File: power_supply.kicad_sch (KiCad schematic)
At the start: 4 parts

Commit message: All component except led matrix
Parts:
- gave numbers to parts that had none: 4
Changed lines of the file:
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@@
   (junction (at 31.75 41.275) (diameter 0) (color 0 0 0 0)
-  )
-  (junction (at 27.94 41.275) (diameter 0) (color 0 0 0 0)
   )
   (junction (at 71.12 41.275) (diameter 0) (color 0 0 0 0)
@@
   )
   (wire (pts (xy 71.12 41.275) (xy 76.2 41.275))
-    (stroke (width 0) (type default) (color 0 0 0 0))
-  )
-  (wire (pts (xy 26.67 41.275) (xy 27.94 41.275))
     (stroke (width 0) (type default) (color 0 0 0 0))
   )
@@
   (symbol (lib_id "Device:C") (at 31.75 46.355 0) (unit 1)
     (in_bom yes) (on_board yes) (fields_autoplaced)
-    (property "Reference" "C?" (id 0) (at 35.56 45.0849 0)
+    (property "Reference" "C1" (id 0) (at 35.56 45.0849 0)
       (effects (font (size 1.27 1.27)) (justify left))
     )
@@
   (symbol (lib_id "Device:R") (at 45.72 43.815 90) (unit 1)
     (in_bom yes) (on_board yes) (fields_autoplaced)
-    (property "Reference" "R?" (id 0) (at 45.72 37.465 90))
+    (property "Reference" "R1" (id 0) (at 45.72 37.465 90))
     (property "Value" "10k" (id 1) (at 45.72 40.005 90))
     (property "Footprint" "" (id 2) (at 45.72 45.593 90)
@@
   (symbol (lib_id "Device:C") (at 71.12 46.355 0) (unit 1)
     (in_bom yes) (on_board yes) (fields_autoplaced)
-    (property "Reference" "C?" (id 0) (at 74.93 45.0849 0)
+    (property "Reference" "C2" (id 0) (at 74.93 45.0849 0)
       (effects (font (size 1.27 1.27)) (justify left))
     )
@@
   (symbol (lib_id "Regulator_Linear:AP2112K-3.3") (at 58.42 43.815 0) (unit 1)
     (in_bom yes) (on_board yes) (fields_autoplaced)
-    (property "Reference" "U?" (id 0) (at 58.42 33.655 0))
+    (property "Reference" "U1" (id 0) (at 58.42 33.655 0))
     (property "Value" "AP2112K-3.3" (id 1) (at 58.42 36.195 0))
     (property "Footprint" "Package_TO_SOT_SMD:SOT-23-5" (id 2) (at 58.42 35.56 0)

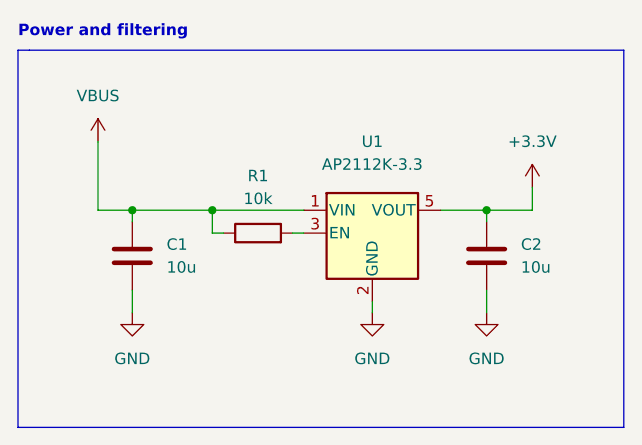
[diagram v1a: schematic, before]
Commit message: finish schematic, prep pcb
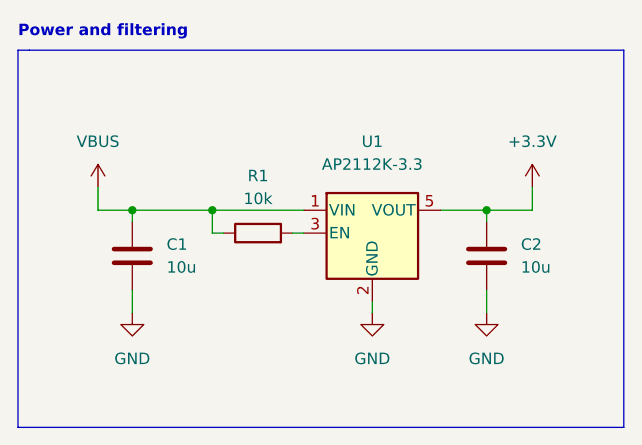
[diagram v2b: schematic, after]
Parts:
- C1, C2: footprint (none) -> Capacitor_SMD:C_0603_1608Metric
- R1: footprint (none) -> Resistor_SMD:R_0402_1005Metric
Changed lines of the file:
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@@
     (stroke (width 0) (type default) (color 0 0 0 0))
   )
-  (wire (pts (xy 27.94 33.655) (xy 27.94 41.275))
+  (wire (pts (xy 27.94 38.735) (xy 27.94 41.275))
     (stroke (width 0) (type default) (color 0 0 0 0))
   )
@@
       (effects (font (size 1.27 1.27)) (justify left))
     )
-    (property "Footprint" "" (id 2) (at 32.7152 50.165 0)
+    (property "Footprint" "Capacitor_SMD:C_0603_1608Metric" (id 2) (at 32.7152 50.165 0)
       (effects (font (size 1.27 1.27)) hide)
     )
@@
     (property "Reference" "R1" (id 0) (at 45.72 37.465 90))
     (property "Value" "10k" (id 1) (at 45.72 40.005 90))
-    (property "Footprint" "" (id 2) (at 45.72 45.593 90)
+    (property "Footprint" "Resistor_SMD:R_0402_1005Metric" (id 2) (at 45.72 45.593 90)
       (effects (font (size 1.27 1.27)) hide)
     )
@@
       (effects (font (size 1.27 1.27)) (justify left))
     )
-    (property "Footprint" "" (id 2) (at 72.0852 50.165 0)
+    (property "Footprint" "Capacitor_SMD:C_0603_1608Metric" (id 2) (at 72.0852 50.165 0)
       (effects (font (size 1.27 1.27)) hide)
     )
@@
   (symbol (lib_id "power:GND") (at 71.12 52.705 0) (unit 1)
     (in_bom yes) (on_board yes) (fields_autoplaced)
-    (property "Reference" "#PWR0105" (id 0) (at 71.12 59.055 0)
+    (property "Reference" "#PWR05" (id 0) (at 71.12 59.055 0)
       (effects (font (size 1.27 1.27)) hide)
     )
@@
   (symbol (lib_id "power:GND") (at 58.42 52.705 0) (unit 1)
     (in_bom yes) (on_board yes) (fields_autoplaced)
-    (property "Reference" "#PWR0103" (id 0) (at 58.42 59.055 0)
+    (property "Reference" "#PWR04" (id 0) (at 58.42 59.055 0)
       (effects (font (size 1.27 1.27)) hide)
     )
@@
   (symbol (lib_id "power:GND") (at 31.75 52.705 0) (unit 1)
     (in_bom yes) (on_board yes) (fields_autoplaced)
-    (property "Reference" "#PWR0101" (id 0) (at 31.75 59.055 0)
+    (property "Reference" "#PWR03" (id 0) (at 31.75 59.055 0)
       (effects (font (size 1.27 1.27)) hide)
     )
@@
     (pin "1")
   )
-  (symbol (lib_id "power:VBUS") (at 27.94 33.655 0) (mirror y) (unit 1)
+  (symbol (lib_id "power:VBUS") (at 27.94 38.735 0) (mirror y) (unit 1)
     (in_bom yes) (on_board yes) (fields_autoplaced)
-    (property "Reference" "#PWR0102" (id 0) (at 27.94 37.465 0)
+    (property "Reference" "#PWR01" (id 0) (at 27.94 42.545 0)
       (effects (font (size 1.27 1.27)) hide)
     )
-    (property "Value" "VBUS" (id 1) (at 27.94 28.575 0))
-    (property "Footprint" "" (id 2) (at 27.94 33.655 0)
+    (property "Value" "VBUS" (id 1) (at 27.94 33.655 0))
+    (property "Footprint" "" (id 2) (at 27.94 38.735 0)
       (effects (font (size 1.27 1.27)) hide)
     )
-    (property "Datasheet" "" (id 3) (at 27.94 33.655 0)
+    (property "Datasheet" "" (id 3) (at 27.94 38.735 0)
       (effects (font (size 1.27 1.27)) hide)
     )
@@
   (symbol (lib_id "power:+3.3V") (at 76.2 38.735 0) (unit 1)
     (in_bom yes) (on_board yes) (fields_autoplaced)
-    (property "Reference" "#PWR0104" (id 0) (at 76.2 42.545 0)
+    (property "Reference" "#PWR02" (id 0) (at 76.2 42.545 0)
       (effects (font (size 1.27 1.27)) hide)
     )
